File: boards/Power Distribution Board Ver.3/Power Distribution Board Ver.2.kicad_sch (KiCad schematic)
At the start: 74 parts, among them J1 Screw_Terminal_01x02, J4 Screw_Terminal_01x06, U1 SIC431AED-T1-GE3, U2 SIC431AED-T1-GE3, U3 SIC431AED-T1-GE3

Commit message: schematic changes
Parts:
- added F1, F2, F3: 0685P9200-01, IRIS:FUSC3215X83N, symbol IRIS:0685P9200-01
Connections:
- net 5V_OUT_1: now also F3.2; no longer D9.2 (K)
- net 5V_OUT_2: now also F2.2; no longer D7.2 (K)
- net 5V_OUT_3: now also F1.2; no longer D8.2 (K)
- new net: D9.2 (K), F3.1
- new net: D8.2 (K), F1.1
- new net: D7.2 (K), F2.1
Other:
- moved on the sheet: C1, C10, C11, C12, C13, C14, C15, C16, C17, C18, C19, C2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

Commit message: PCBPCB Schematics Done
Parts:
- removed D7, D8, D9: ${SIM.PARAMS}, Package_TO_SOT_SMD:TO-263-2, symbol Simulation_SPICE:DIODE
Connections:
- net at C18.1, C33.1, C34.1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: now also F3.1
- net at C16.1, C26.1, C27.1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: now also F1.1
- net at C17.1, C19.1, C20.1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: now also F2.1
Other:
- moved on the sheet: C11, C14, C17, C19, C2, C20, C21, C22, C23, C24, C25, C5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

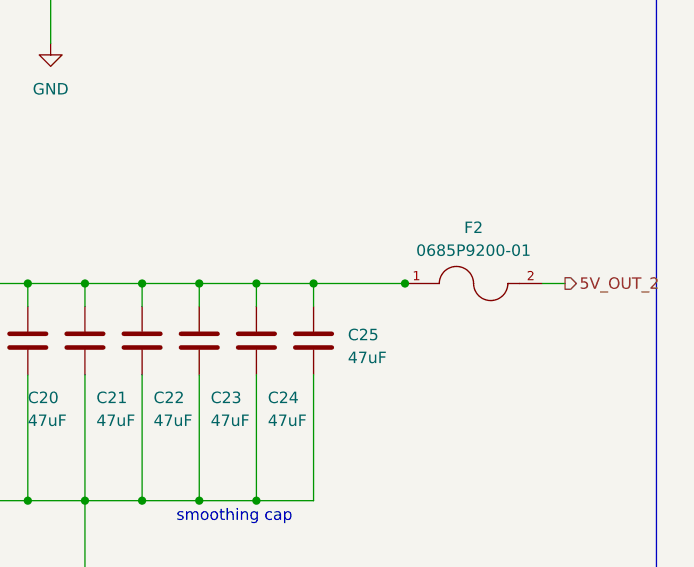
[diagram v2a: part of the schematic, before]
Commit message: 12v relay footprint and updated board wiring
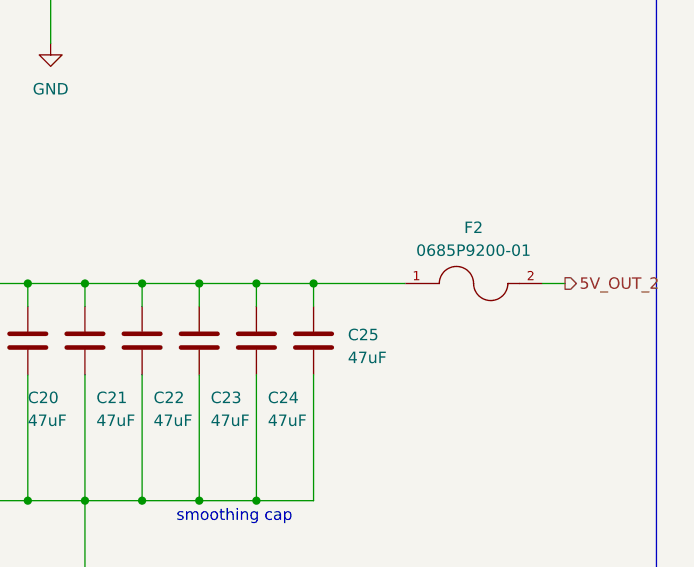
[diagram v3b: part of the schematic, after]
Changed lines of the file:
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@@
-	)
-	(junction
-		(at 227.33 223.52)
-		(diameter 0)
-		(color 0 0 0 0)
 	)
 	(junction
@@
 		)
 		(stroke
-			(width 0)
-			(type default)
-		)
-	)
-	(wire
-		(pts
-			(xy 227.33 223.4692) (xy 227.33 223.52)
-		)
-		(stroke

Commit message: Updated PCBPCB schematic
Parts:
- L1, L2, L3: value 1uH -> 1.2uH
- R16, R17, R18: value 0 -> 3.3
- R22, R23: value 78.7k -> 73.2
- R24: value 78.7k -> 73.2k
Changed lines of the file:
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@@
 			)
 		)
-		(property "Value" "78.7k"
+		(property "Value" "73.2k"
 			(at 153.924 300.99 90)
 			(effects
@@
 			)
 		)
-		(property "Value" "0"
+		(property "Value" "3.3"
 			(at 138.049 154.813 90)
 			(effects
@@
 			)
 		)
-		(property "Value" "78.7k"
+		(property "Value" "73.2"
 			(at 153.162 240.284 90)
 			(effects
@@
 			)
 		)
-		(property "Value" "1uH"
+		(property "Value" "1.2uH"
 			(at 151.257 221.869 90)
 			(effects
@@
 			)
 		)
-		(property "Value" "0"
+		(property "Value" "3.3"
 			(at 138.303 216.154 90)
 			(effects
@@
 			)
 		)
-		(property "Value" "1uH"
+		(property "Value" "1.2uH"
 			(at 151.384 160.528 90)
 			(effects
@@
 			)
 		)
-		(property "Value" "78.7k"
+		(property "Value" "73.2"
 			(at 153.289 178.943 90)
 			(effects
@@
 			)
 		)
-		(property "Value" "0"
+		(property "Value" "3.3"
 			(at 138.811 276.86 90)
 			(effects
@@
 			)
 		)
-		(property "Value" "1uH"
+		(property "Value" "1.2uH"
 			(at 152.019 282.575 90)
 			(effects

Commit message: GL connections and minor trace fixes
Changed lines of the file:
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@@
 (kicad_sch
-	(version 20231120)
+	(version 20250114)
 	(generator "eeschema")
-	(generator_version "8.0")
+	(generator_version "9.0")
 	(paper "A2")
+	(text "power ground"
+		(exclude_from_sim no)
+		(at 122.174 195.453 0)
+		(effects
+			(font
+				(size 1.27 1.27)
+			)
+			(justify left bottom)
+		)
+	)
+	(text "Connectors"
+		(exclude_from_sim no)
+		(at 16.383 20.574 0)
+		(effects
+			(font
+				(size 5 5)
+			)
+			(justify left bottom)
+		)
+	)
+	(text "analog ground"
+		(exclude_from_sim no)
+		(at 101.219 317.5 0)
+		(effects
+			(font
+				(size 1.27 1.27)
+			)
+			(justify left bottom)
+		)
+	)
+	(text "Battery Terminal\n"
+		(exclude_from_sim no)
+		(at 15.367 26.924 0)
+		(effects
+			(font
+				(size 2.54 2.54)
+			)
+			(justify left bottom)
+		)
+	)
+	(text "smoothing cap"
+		(exclude_from_sim no)
+		(at 201.93 250.19 0)
+		(effects
+			(font
+				(size 1.27 1.27)
+			)
+			(justify left bottom)
+		)
+	)
+	(text "5V Terminal"
+		(exclude_from_sim no)
+		(at 15.748 38.1 0)
+		(effects
+			(font
+				(size 2.54 2.54)
+			)
+			(justify left bottom)
+		)
+	)
+	(text "smoothing cap"
+		(exclude_from_sim no)
+		(at 199.39 189.23 0)
+		(effects
+			(font
+				(size 1.27 1.27)
+			)
+			(justify left bottom)
+		)
+	)
+	(text "power ground"
+		(exclude_from_sim no)
+		(at 122.809 317.5 0)
+		(effects
+			(font
+				(size 1.27 1.27)
+			)
+			(justify left bottom)
+		)
+	)
+	(text "smoothing cap"
+		(exclude_from_sim no)
+		(at 199.39 311.15 0)
+		(effects
+			(font
+				(size 1.27 1.27)
+			)
+			(justify left bottom)
+		)
+	)
+	(text "analog ground"
+		(exclude_from_sim no)
+		(at 100.584 195.453 0)
+		(effects
+			(font
+				(size 1.27 1.27)
+			)
+			(justify left bottom)
+		)
+	)
+	(text "3 outputs in total"
+		(exclude_from_sim no)
+		(at 42.418 37.846 0)
+		(effects
+			(font
+				(size 1.27 1.27)
+			)
+			(justify left bottom)
+		)
+	)
+	(text "analog ground"
+		(exclude_from_sim no)
+		(at 100.457 256.794 0)
+		(effects
+			(font
+				(size 1.27 1.27)
+			)
+			(justify left bottom)
+		)
+	)
+	(text "power ground"
+		(exclude_from_sim no)
+		(at 122.047 256.794 0)
+		(effects
+			(font
+				(size 1.27 1.27)
+			)
+			(justify left bottom)
+		)
+	)
+	(text "12 Volt Regulators"
+		(exclude_from_sim no)
+		(at 18.288 139.7 0)
+		(effects
+			(font
+				(size 5 5)
+			)
+			(justify left bottom)
+		)
+	)
 	(junction
 		(at 208.28 284.48)
@@
 		)
 	)
-	(text "power ground"
-		(exclude_from_sim no)
-		(at 122.174 195.453 0)
-		(effects
-			(font
-				(size 1.27 1.27)
-			)
-			(justify left bottom)
-		)
-	)
-	(text "Connectors"
-		(exclude_from_sim no)
-		(at 16.383 20.574 0)
-		(effects
-			(font
-				(size 5 5)
-			)
-			(justify left bottom)
-		)
-	)
-	(text "analog ground"
-		(exclude_from_sim no)
-		(at 101.219 317.5 0)
-		(effects
-			(font
-				(size 1.27 1.27)
-			)
-			(justify left bottom)
-		)
-	)
-	(text "Battery Terminal\n"
-		(exclude_from_sim no)
-		(at 15.367 26.924 0)
-		(effects
-			(font
-				(size 2.54 2.54)
-			)
-			(justify left bottom)
-		)
-	)
-	(text "smoothing cap"
-		(exclude_from_sim no)
-		(at 201.93 250.19 0)
-		(effects
-			(font
-				(size 1.27 1.27)
-			)
-			(justify left bottom)
-		)
-	)
-	(text "5V Terminal"
-		(exclude_from_sim no)
-		(at 15.748 38.1 0)
-		(effects
-			(font
-				(size 2.54 2.54)
-			)
-			(justify left bottom)
-		)
-	)
-	(text "smoothing cap"
-		(exclude_from_sim no)
-		(at 199.39 189.23 0)
-		(effects
-			(font
-				(size 1.27 1.27)
-			)
-			(justify left bottom)
-		)
-	)
-	(text "power ground"
-		(exclude_from_sim no)
-		(at 122.809 317.5 0)
-		(effects
-			(font
-				(size 1.27 1.27)
-			)
-			(justify left bottom)
-		)
-	)
-	(text "smoothing cap"
-		(exclude_from_sim no)
-		(at 199.39 311.15 0)
-		(effects
-			(font
-				(size 1.27 1.27)
-			)
-			(justify left bottom)
-		)
-	)
-	(text "analog ground"
-		(exclude_from_sim no)
-		(at 100.584 195.453 0)
-		(effects
-			(font
-				(size 1.27 1.27)
-			)
-			(justify left bottom)
-		)
-	)
-	(text "3 outputs in total"
-		(exclude_from_sim no)
-		(at 42.418 37.846 0)
-		(effects
-			(font
-				(size 1.27 1.27)
-			)
-			(justify left bottom)
-		)
-	)
-	(text "analog ground"
-		(exclude_from_sim no)
-		(at 100.457 256.794 0)
-		(effects
-			(font
-				(size 1.27 1.27)
-			)
-			(justify left bottom)
-		)
-	)
-	(text "power ground"
-		(exclude_from_sim no)
-		(at 122.047 256.794 0)
-		(effects
-			(font
-				(size 1.27 1.27)
-			)
-			(justify left bottom)
-		)
-	)
-	(text "12 Volt Regulators"
-		(exclude_from_sim no)
-		(at 18.288 139.7 0)
-		(effects
-			(font
-				(size 5 5)
-			)
-			(justify left bottom)
-		)
-	)
 	(hierarchical_label "GND"
 		(shape input)
 		(at 39.37 54.61 180)
-		(fields_autoplaced yes)
 		(effects
 			(font
@@
 		(shape input)
 		(at 39.37 52.07 180)
-		(fields_autoplaced yes)
 		(effects
 			(font
@@
 		(shape output)
 		(at 245.11 223.52 0)
-		(fields_autoplaced yes)
 		(effects
 			(font
@@
 		(shape input)
 		(at 39.37 49.53 180)
-		(fields_autoplaced yes)
 		(effects
 			(font
@@
 		(shape output)
 		(at 137.414 289.56 0)
-		(fields_autoplaced yes)
 		(effects
 			(font
@@
 		(shape input)
 		(at 39.37 41.91 180)
-		(fields_autoplaced yes)
 		(effects
 			(font
@@
 		(shape output)
 		(at 38.862 32.004 180)
-		(fields_autoplaced yes)
 		(effects
 			(font
@@
 		(shape input)
 		(at 26.289 157.353 180)
-		(fields_autoplaced yes)
 		(effects
 			(font
@@
 		(shape input)
 		(at 26.924 279.4 180)
-		(fields_autoplaced yes)
 		(effects
 			(font
@@
 		(shape output)
 		(at 136.652 228.854 0)
-		(fields_autoplaced yes)
 		(effects
 			(font
@@
 		(shape output)
 		(at 243.84 284.48 0)
-		(fields_autoplaced yes)
 		(effects
 			(font
@@
 		(shape output)
 		(at 241.4016 162.687 0)
-		(fields_autoplaced yes)
 		(effects
 			(font
@@
 		(shape input)
 		(at 39.37 44.45 180)
-		(fields_autoplaced yes)
 		(effects
 			(font
@@
 		(shape output)
 		(at 136.779 167.513 0)
-		(fields_autoplaced yes)
 		(effects
 			(font
@@
 		(shape input)
 		(at 39.37 46.99 180)
-		(fields_autoplaced yes)
 		(effects
 			(font
@@
 		(shape input)
 		(at 38.862 29.464 180)
-		(fields_autoplaced yes)
 		(effects
 			(font
@@
 		(shape input)
 		(at 26.162 218.694 180)
-		(fields_autoplaced yes)
 		(effects
 			(font
@@
 		)
 	)
+	(embedded_fonts no)
 )
